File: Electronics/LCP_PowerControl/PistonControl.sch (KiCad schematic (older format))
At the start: 11 parts, among them J3 Conn_01x02, U2 DRV8874

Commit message: Adding libraries and recent changes
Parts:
- removed J3: Conn_01x02, symbol Connector_Generic:Conn_01x02
- added J?: Conn_02x04_Odd_Even, Connector_PinSocket_2.54mm:PinSocket_2x04_P2.54mm_Vertical, symbol Connector_Generic:Conn_02x04_Odd_Even
- added TP? (x4): TestPoint, TestPoint:TestPoint_Keystone_5000-5004_Miniature, symbol Connector:TestPoint
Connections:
- net GND: now also J?.2 (Pin_2), J?.4 (Pin_4), J?.6 (Pin_6), J?.8 (Pin_8)
- net MD_EN: now also J?.1 (Pin_1)
- net MD_IPROPI: now also TP?.1
- net MD_PH: now also J?.3 (Pin_3)
- net MD_PMODE: now also J?.7 (Pin_7)
- net V_ref: now also TP?.1
- net ~MD_FAULT: now also J?.5 (Pin_5)
- net ACTUATOR_POWER-: now reaches U2.10 (OUT2)
- net ACTUATOR_POWER-: now also TP?.1
- net ACTUATOR_POWER+: now reaches U2.8 (OUT1)
- net ACTUATOR_POWER+: now also TP?.1
- net +BATT renamed +12V
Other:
- note removed: "TO 12VDC BLDC MOTOR"
- moved on the sheet: C4, C5, C6, C7, F2, R10, R11, R12, R9, U2

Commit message: Aiming for rev 0.1 complete
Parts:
- removed F2: Polyfuse, symbol Device:Polyfuse
- C4: footprint (none) -> Capacitor_THT:CP_Radial_D12.5mm_P5.00mm; MPN (none) -> UVR1H102MHD
- gave numbers to parts that had none: 5
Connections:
- net +12V: now also C4.1, C5.1, C6.1, U2.11 (VM)
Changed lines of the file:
@@
 Sheet 6 11
 Title ""
-Date ""
-Rev ""
+Date "2020-06-17"
+Rev "R0.1"
 Comp ""
-Comment1 ""
+Comment1 "Design by: Matt Casari"
 Comment2 ""
 Comment3 ""
@@
 $EndComp
 Wire Wire Line
-	5600 2250 5850 2250
-Wire Wire Line
 	5850 2250 6250 2250
 $Comp
@@
 F 0 "C4" H 5968 2546 50  0000 L CNN
 F 1 "CP" H 5968 2455 50  0000 L CNN
-F 2 "" H 5888 2350 50  0001 C CNN
+F 2 "Capacitor_THT:CP_Radial_D12.5mm_P5.00mm" H 5888 2350 50  0001 C CNN
 F 3 "~" H 5850 2500 50  0001 C CNN
+F 4 "UVR1H102MHD" H 5850 2500 50  0001 C CNN "MPN"
 	1    5850 2500
 	1    0    0    -1
@@
 Wire Wire Line
 	5850 2750 5850 2650
-$Comp
-L Device:Polyfuse F2
-U 1 1 5EE55CEE
-P 5450 2250
-F 0 "F2" V 5225 2250 50  0000 C CNN
-F 1 "Polyfuse" V 5316 2250 50  0000 C CNN
-F 2 "" H 5500 2050 50  0001 L CNN
-F 3 "~" H 5450 2250 50  0001 C CNN
-	1    5450 2250
-	0    1    1    0
-$EndComp
 Wire Wire Line
 	5150 2250 5150 2000
@@
 Wire Wire Line
 	6250 2250 6900 2250
-Wire Wire Line
-	5300 2250 5150 2250
 Wire Wire Line
 	7100 2500 7100 2250
@@
 P 3000 5300
 AR Path="/5EE2AA1B/5EF03805" Ref="#PWR?"  Part="1"
-AR Path="/5EE2AB43/5EF03805" Ref="#PWR?"  Part="1"
-F 0 "#PWR?" H 3000 5050 50  0001 C CNN
+AR Path="/5EE2AB43/5EF03805" Ref="#PWR035"  Part="1"
+F 0 "#PWR035" H 3000 5050 50  0001 C CNN
 F 1 "GND" H 3005 5127 50  0000 C CNN
 F 2 "" H 3000 5300 50  0001 C CNN
@@
 P 3100 4850
 AR Path="/5EE2AA1B/5EF03813" Ref="J?"  Part="1"
-AR Path="/5EE2AB43/5EF03813" Ref="J?"  Part="1"
-F 0 "J?" V 3059 4562 50  0000 R CNN
+AR Path="/5EE2AB43/5EF03813" Ref="J16"  Part="1"
+F 0 "J16" V 3059 4562 50  0000 R CNN
 F 1 "Conn_02x04_Odd_Even" V 3150 4562 50  0000 R CNN
 F 2 "Connector_PinSocket_2.54mm:PinSocket_2x04_P2.54mm_Vertical" H 3100 4850 50  0001 C CNN
@@
 	3200 4650 3200 3600
 $Comp
-L Connector:TestPoint TP?
+L Connector:TestPoint TP5
 U 1 1 5EF1DD9D
 P 8400 3650
-F 0 "TP?" H 8458 3768 50  0000 L CNN
+F 0 "TP5" H 8458 3768 50  0000 L CNN
 F 1 "TestPoint" H 8458 3677 50  0000 L CNN
 F 2 "TestPoint:TestPoint_Keystone_5000-5004_Miniature" H 8600 3650 50  0001 C CNN
@@
 	8400 3750 9350 3750
 $Comp
-L Connector:TestPoint TP?
+L Connector:TestPoint TP6
 U 1 1 5EF21475
 P 8850 3650
-F 0 "TP?" H 8908 3768 50  0000 L CNN
+F 0 "TP6" H 8908 3768 50  0000 L CNN
 F 1 "TestPoint" H 8908 3677 50  0000 L CNN
 F 2 "TestPoint:TestPoint_Keystone_5000-5004_Miniature" H 9050 3650 50  0001 C CNN
@@
 	9350 3900 9900 3900
 $Comp
-L power:+12V #PWR?
+L power:+12V #PWR036
 U 1 1 5EEFB289
 P 5150 2000
-F 0 "#PWR?" H 5150 1850 50  0001 C CNN
+F 0 "#PWR036" H 5150 1850 50  0001 C CNN
 F 1 "+12V" H 5165 2173 50  0000 C CNN
 F 2 "" H 5150 2000 50  0001 C CNN
@@
 $EndComp
 $Comp
-L Connector:TestPoint TP?
+L Connector:TestPoint TP4
 U 1 1 5EF070DA
 P 4900 3800
-F 0 "TP?" H 4958 3918 50  0000 L CNN
+F 0 "TP4" H 4958 3918 50  0000 L CNN
 F 1 "TestPoint" H 4958 3827 50  0000 L CNN
 F 2 "TestPoint:TestPoint_Keystone_5000-5004_Miniature" H 5100 3800 50  0001 C CNN
@@
 $EndComp
 $Comp
-L Connector:TestPoint TP?
+L Connector:TestPoint TP3
 U 1 1 5EF092C0
 P 4500 5450
-F 0 "TP?" H 4558 5568 50  0000 L CNN
+F 0 "TP3" H 4558 5568 50  0000 L CNN
 F 1 "TestPoint" H 4558 5477 50  0000 L CNN
 F 2 "TestPoint:TestPoint_Keystone_5000-5004_Miniature" H 4700 5450 50  0001 C CNN
@@
 Wire Wire Line
 	1950 4250 3300 4250
+Wire Wire Line
+	5150 2250 5850 2250
 $EndSCHEMATC

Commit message: LCP_PowerControl Rev1
Board layout in Kicad.
Gerbers.
BOM
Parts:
- C5, C6: MPN (none) -> 885012207045
- C7: MPN (none) -> 885342207006
- R10: MPN (none) -> RNCP0805FTD10K0
- R11: MPN (none) -> RNCP0805FTD1K30
- R12: MPN (none) -> RNCP0805FTD2K00
- R9: MPN (none) -> CRG0805F750R
- U2: MPN (none) -> DRV8874PWPR
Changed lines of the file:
@@
 F 2 "Package_SO:HTSSOP-16-1EP_4.4x5mm_P0.65mm_EP3.4x5mm_Mask3x3mm_ThermalVias" H 7050 2800 50  0001 C CNN
 F 3 "https://www.ti.com/lit/ds/symlink/drv8874.pdf?ts=1591932536319&ref_url=https%253A%252F%252Fwww.ti.com%252Fproduct%252FDRV8874%253FkeyMatch%253DDRV8874%2526tisearch%253DSearch-EN-everything%2526usecase%253DGPN" H 6900 4450 50  0001 C CNN
+F 4 "DRV8874PWPR" H 6950 3750 50  0001 C CNN "MPN"
 	1    6950 3750
 	1    0    0    -1
@@
 F 2 "Resistor_SMD:R_0805_2012Metric" V 5080 5850 50  0001 C CNN
 F 3 "~" H 5150 5850 50  0001 C CNN
+F 4 "RNCP0805FTD2K00" H 5150 5850 50  0001 C CNN "MPN"
 	1    5150 5850
 	1    0    0    -1
@@
 F 2 "Resistor_SMD:R_0805_2012Metric" V 5080 5350 50  0001 C CNN
 F 3 "~" H 5150 5350 50  0001 C CNN
+F 4 "RNCP0805FTD1K30" H 5150 5350 50  0001 C CNN "MPN"
 	1    5150 5350
 	1    0    0    -1
@@
 F 2 "Resistor_SMD:R_0805_2012Metric" V 4280 2900 50  0001 C CNN
 F 3 "~" H 4350 2900 50  0001 C CNN
+F 4 "RNCP0805FTD10K0" H 4350 2900 50  0001 C CNN "MPN"
 	1    4350 2900
 	1    0    0    -1
@@
 F 2 "Resistor_SMD:R_0805_2012Metric" V 4280 4500 50  0001 C CNN
 F 3 "~" H 4350 4500 50  0001 C CNN
+F 4 "CRG0805F750R" H 4350 4500 50  0001 C CNN "MPN"
 	1    4350 4500
 	1    0    0    -1
@@
 F 2 "Capacitor_SMD:C_0805_2012Metric" H 8238 3000 50  0001 C CNN
 F 3 "~" H 8200 3150 50  0001 C CNN
+F 4 "885342207006" H 8200 3150 50  0001 C CNN "MPN"
 	1    8200 3150
 	1    0    0    -1
@@
 F 4 "16V" H 7100 2650 50  0001 C CNN "VR"
 F 5 "X7R" H 7100 2650 50  0001 C CNN "Type"
-F 6 "" H 7100 2650 50  0001 C CNN "MPN"
+F 6 "885012207045" H 7100 2650 50  0001 C CNN "MPN"
 	1    7100 2650
 	1    0    0    -1
@@
 F 2 "Capacitor_SMD:C_0805_2012Metric" H 6288 2350 50  0001 C CNN
 F 3 "~" H 6250 2500 50  0001 C CNN
+F 4 "885012207045" H 6250 2500 50  0001 C CNN "MPN"
 	1    6250 2500
 	1    0    0    -1

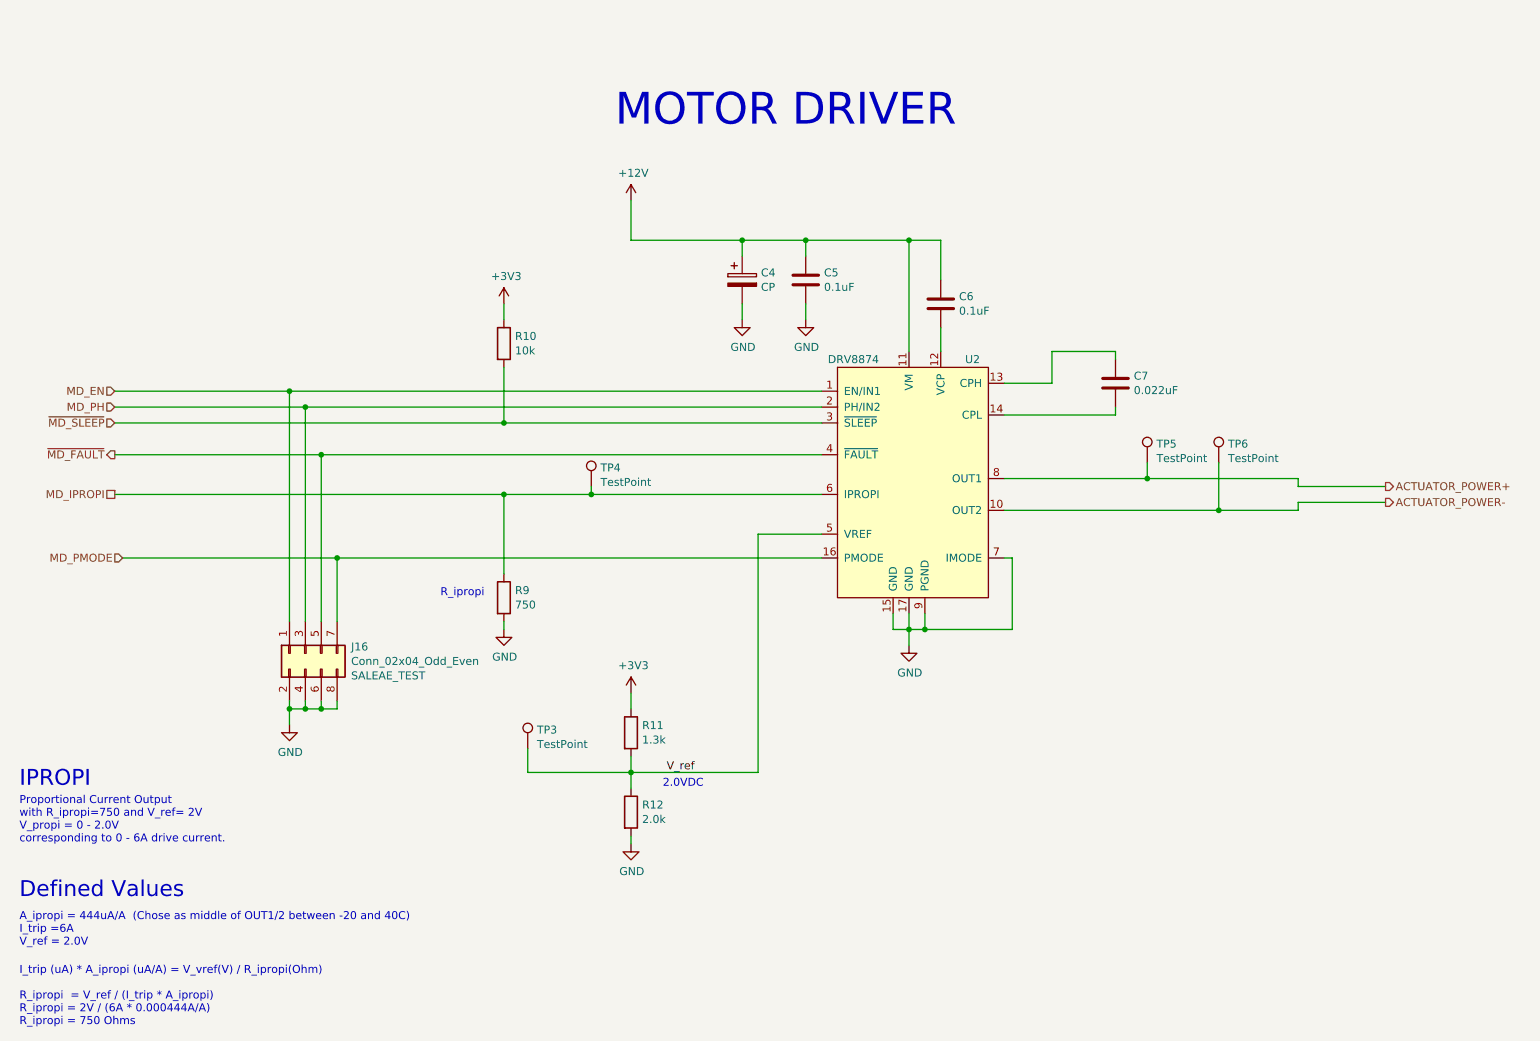
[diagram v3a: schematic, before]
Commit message: Rev1
Removed test points. Cleaned up unnecessary traces. Fixed electrical issues #1-#7
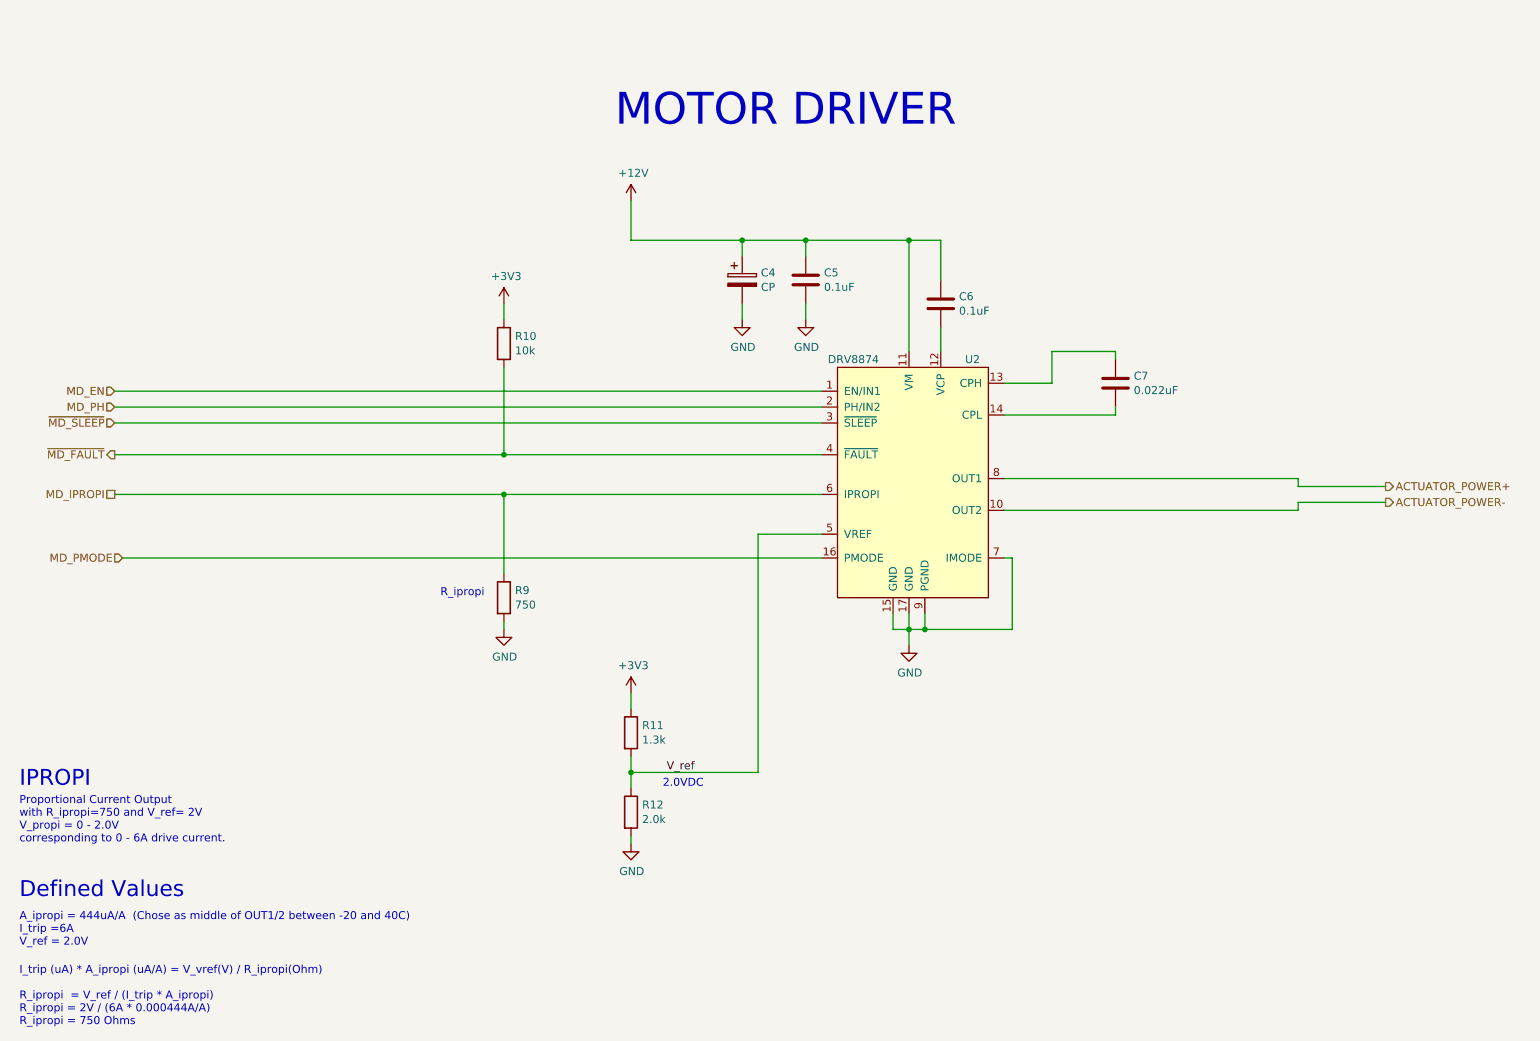
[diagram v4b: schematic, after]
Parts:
- removed J16: Conn_02x04_Odd_Even, Connector_PinSocket_2.54mm:PinSocket_2x04_P2.54mm_Vertical, symbol Connector_Generic:Conn_02x04_Odd_Even
- removed TP3, TP4, TP5, TP6: TestPoint, TestPoint:TestPoint_Keystone_5000-5004_Miniature, symbol Connector:TestPoint
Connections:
- net ~MD_FAULT: now also R10.2
- net ~MD_SLEEP: no longer R10.2
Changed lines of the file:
@@
 	1    0    0    -1
 $EndComp
-Wire Wire Line
-	6350 3400 4350 3400
-Wire Wire Line
-	4350 3400 4350 3050
 $Comp
 L power:+3V3 #PWR012
@@
 MD_PMODE
 Wire Wire Line
-	6350 3300 3100 3300
-Wire Wire Line
-	6350 3850 4900 3850
-Wire Wire Line
 	4350 4350 4350 3850
 Connection ~ 4350 3850
 Text HLabel 1900 3400 0    50   Input ~ 0
 ~MD_SLEEP
-Wire Wire Line
-	1900 3400 4350 3400
-Connection ~ 4350 3400
 $Comp
 L Device:C C7
@@
 Wire Wire Line
 	9350 3900 9350 3950
-Wire Wire Line
-	9350 3950 8850 3950
-Wire Wire Line
-	7500 3750 8400 3750
 Wire Wire Line
 	9350 3750 9350 3800
@@
 Text Notes 1300 5700 0    100  ~ 0
 IPROPI
-$Comp
-L power:GND #PWR?
-U 1 1 5EF03805
-P 3000 5300
-AR Path="/5EE2AA1B/5EF03805" Ref="#PWR?"  Part="1"
-AR Path="/5EE2AB43/5EF03805" Ref="#PWR035"  Part="1"
-F 0 "#PWR035" H 3000 5050 50  0001 C CNN
-F 1 "GND" H 3005 5127 50  0000 C CNN
-F 2 "" H 3000 5300 50  0001 C CNN
-F 3 "" H 3000 5300 50  0001 C CNN
-	1    3000 5300
-	1    0    0    -1
-$EndComp
-Wire Wire Line
-	3000 5300 3000 5200
-Wire Wire Line
-	3100 5150 3100 5200
-Wire Wire Line
-	3100 5200 3000 5200
-Connection ~ 3000 5200
-Wire Wire Line
-	3000 5200 3000 5150
-Wire Wire Line
-	3200 5150 3200 5200
-Connection ~ 3100 5200
-$Comp
-L Connector_Generic:Conn_02x04_Odd_Even J?
-U 1 1 5EF03813
-P 3100 4850
-AR Path="/5EE2AA1B/5EF03813" Ref="J?"  Part="1"
-AR Path="/5EE2AB43/5EF03813" Ref="J16"  Part="1"
-F 0 "J16" V 3059 4562 50  0000 R CNN
-F 1 "Conn_02x04_Odd_Even" V 3150 4562 50  0000 R CNN
-F 2 "Connector_PinSocket_2.54mm:PinSocket_2x04_P2.54mm_Vertical" H 3100 4850 50  0001 C CNN
-F 3 "~" H 3100 4850 50  0001 C CNN
-F 4 "SALEAE_TEST" V 3241 4562 50  0000 R CNN "Field4"
-	1    3100 4850
-	0    -1   1    0
-$EndComp
-Wire Wire Line
-	3300 5150 3300 5200
-Wire Wire Line
-	3100 5200 3200 5200
-Wire Wire Line
-	3200 5200 3300 5200
-Connection ~ 3200 5200
-Wire Wire Line
-	3000 4650 3000 3200
-Wire Wire Line
-	3100 4650 3100 3300
-Wire Wire Line
-	3200 4650 3200 3600
-$Comp
-L Connector:TestPoint TP5
-U 1 1 5EF1DD9D
-P 8400 3650
-F 0 "TP5" H 8458 3768 50  0000 L CNN
-F 1 "TestPoint" H 8458 3677 50  0000 L CNN
-F 2 "TestPoint:TestPoint_Keystone_5000-5004_Miniature" H 8600 3650 50  0001 C CNN
-F 3 "~" H 8600 3650 50  0001 C CNN
-	1    8400 3650
-	1    0    0    -1
-$EndComp
-Wire Wire Line
-	8400 3650 8400 3750
-Connection ~ 8400 3750
-Wire Wire Line
-	8400 3750 9350 3750
-$Comp
-L Connector:TestPoint TP6
-U 1 1 5EF21475
-P 8850 3650
-F 0 "TP6" H 8908 3768 50  0000 L CNN
-F 1 "TestPoint" H 8908 3677 50  0000 L CNN
-F 2 "TestPoint:TestPoint_Keystone_5000-5004_Miniature" H 9050 3650 50  0001 C CNN
-F 3 "~" H 9050 3650 50  0001 C CNN
-	1    8850 3650
-	1    0    0    -1
-$EndComp
-Wire Wire Line
-	8850 3650 8850 3950
-Connection ~ 8850 3950
-Wire Wire Line
-	8850 3950 7500 3950
 Text HLabel 9900 3800 2    50   Output ~ 0
 ACTUATOR_POWER+
@@
 	1    0    0    -1
 $EndComp
-$Comp
-L Connector:TestPoint TP4
-U 1 1 5EF070DA
-P 4900 3800
-F 0 "TP4" H 4958 3918 50  0000 L CNN
-F 1 "TestPoint" H 4958 3827 50  0000 L CNN
-F 2 "TestPoint:TestPoint_Keystone_5000-5004_Miniature" H 5100 3800 50  0001 C CNN
-F 3 "~" H 5100 3800 50  0001 C CNN
-	1    4900 3800
-	1    0    0    -1
-$EndComp
-$Comp
-L Connector:TestPoint TP3
-U 1 1 5EF092C0
-P 4500 5450
-F 0 "TP3" H 4558 5568 50  0000 L CNN
-F 1 "TestPoint" H 4558 5477 50  0000 L CNN
-F 2 "TestPoint:TestPoint_Keystone_5000-5004_Miniature" H 4700 5450 50  0001 C CNN
-F 3 "~" H 4700 5450 50  0001 C CNN
-	1    4500 5450
-	1    0    0    -1
-$EndComp
-Wire Wire Line
-	4500 5450 4500 5600
-Wire Wire Line
-	4500 5600 5150 5600
 Wire Wire Line
 	1900 3850 4350 3850
 Wire Wire Line
-	4900 3800 4900 3850
-Connection ~ 4900 3850
-Wire Wire Line
-	4900 3850 4350 3850
-Wire Wire Line
-	3300 4650 3300 4250
-Wire Wire Line
 	5950 5600 5150 5600
-Connection ~ 3000 3200
-Wire Wire Line
-	3000 3200 6350 3200
-Connection ~ 3100 3300
-Connection ~ 3200 3600
-Wire Wire Line
-	3200 3600 6350 3600
-Connection ~ 3300 4250
-Wire Wire Line
-	3300 4250 6350 4250
-Wire Wire Line
-	1900 3200 3000 3200
-Wire Wire Line
-	1900 3600 3200 3600
-Wire Wire Line
-	1900 3300 3100 3300
-Wire Wire Line
-	1950 4250 3300 4250
 Wire Wire Line
 	5150 2250 5850 2250
+Wire Wire Line
+	1900 3400 6350 3400
+Wire Wire Line
+	4350 3050 4350 3600
+Connection ~ 4350 3600
+Wire Wire Line
+	4350 3600 6350 3600
+Wire Wire Line
+	1900 3200 6350 3200
+Wire Wire Line
+	1900 3300 6350 3300
+Wire Wire Line
+	1900 3600 4350 3600
+Wire Wire Line
+	1950 4250 6350 4250
+Wire Wire Line
+	7500 3750 9350 3750
+Wire Wire Line
+	7500 3950 9350 3950
+Wire Wire Line
+	4350 3850 6350 3850
 $EndSCHEMATC

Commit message: LCP PowerControl Board Update
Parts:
- C4: MPN UVR1H102MHD -> ECA-1HM102B
- C7: MPN 885342207006 -> C2012X7R2E223K125AA
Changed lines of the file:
@@
 F 2 "Capacitor_SMD:C_0805_2012Metric" H 8238 3000 50  0001 C CNN
 F 3 "~" H 8200 3150 50  0001 C CNN
-F 4 "885342207006" H 8200 3150 50  0001 C CNN "MPN"
+F 4 "C2012X7R2E223K125AA" H 8200 3150 50  0001 C CNN "MPN"
 	1    8200 3150
 	1    0    0    -1
@@
 F 2 "Capacitor_THT:CP_Radial_D12.5mm_P5.00mm" H 5888 2350 50  0001 C CNN
 F 3 "~" H 5850 2500 50  0001 C CNN
-F 4 "UVR1H102MHD" H 5850 2500 50  0001 C CNN "MPN"
+F 4 "ECA-1HM102B" H 5850 2500 50  0001 C CNN "MPN"
 	1    5850 2500
 	1    0    0    -1
